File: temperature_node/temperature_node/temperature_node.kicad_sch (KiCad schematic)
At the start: 36 parts, among them J1 USB_C_Receptacle_USB2.0_16P, J2 S2B-PH-K-S, U1 ESP32-C3-WROOM-02, U2 SHT40-AD1B-R3, U3 MCP73831-2-OT, U4 USBLC6-2P6, U5 MIC5504-3.3YM5

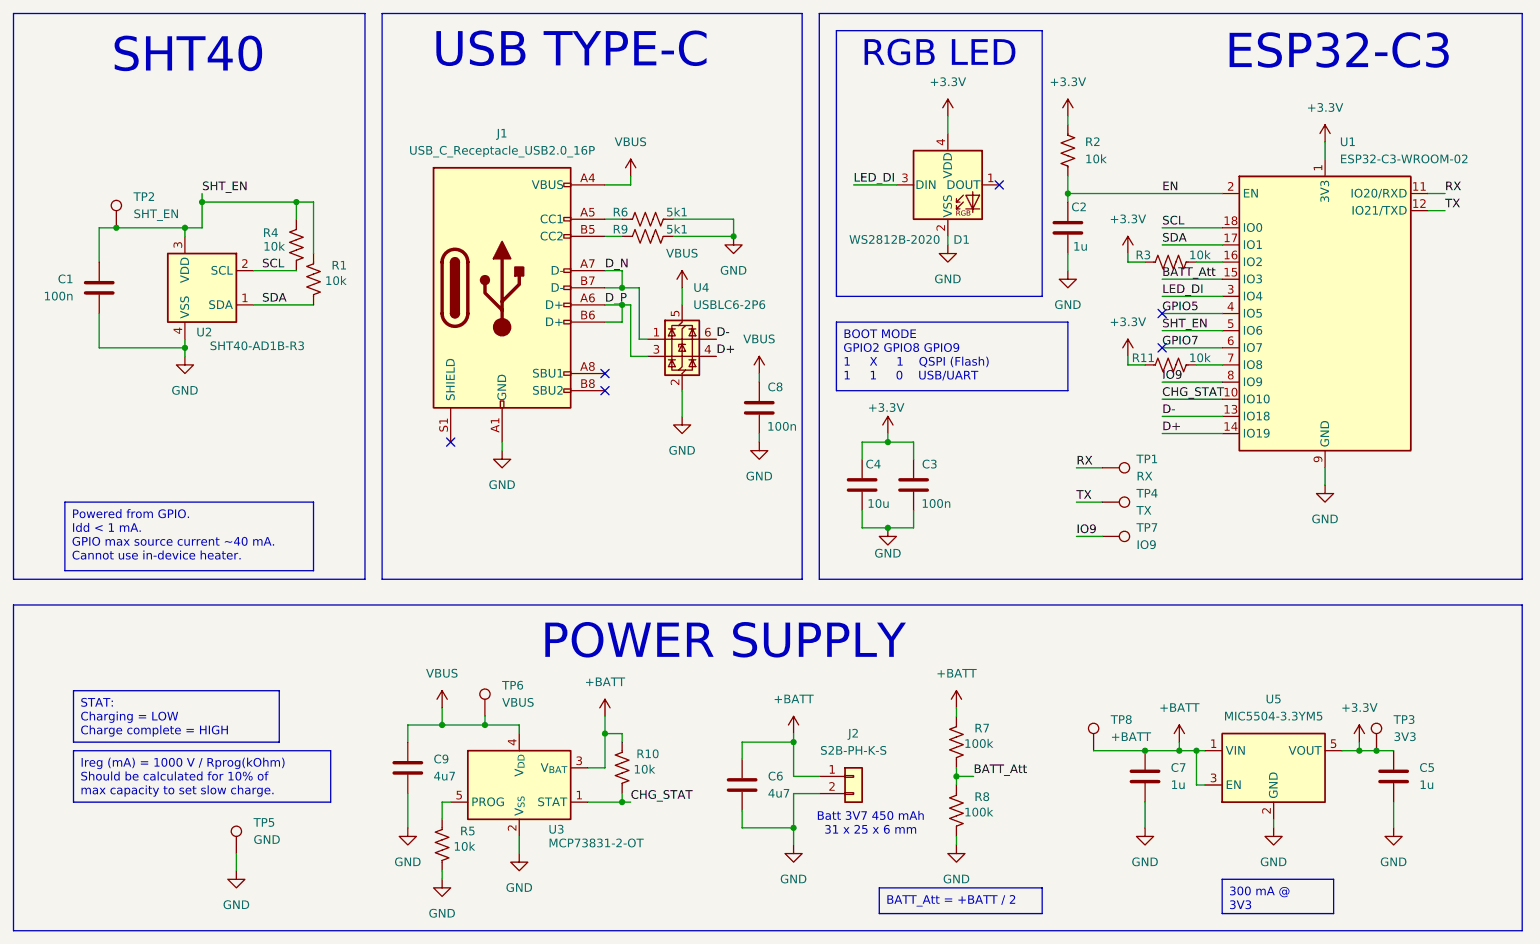
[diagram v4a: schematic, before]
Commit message: Add parameter for BOM and change some cap sizes for better availability
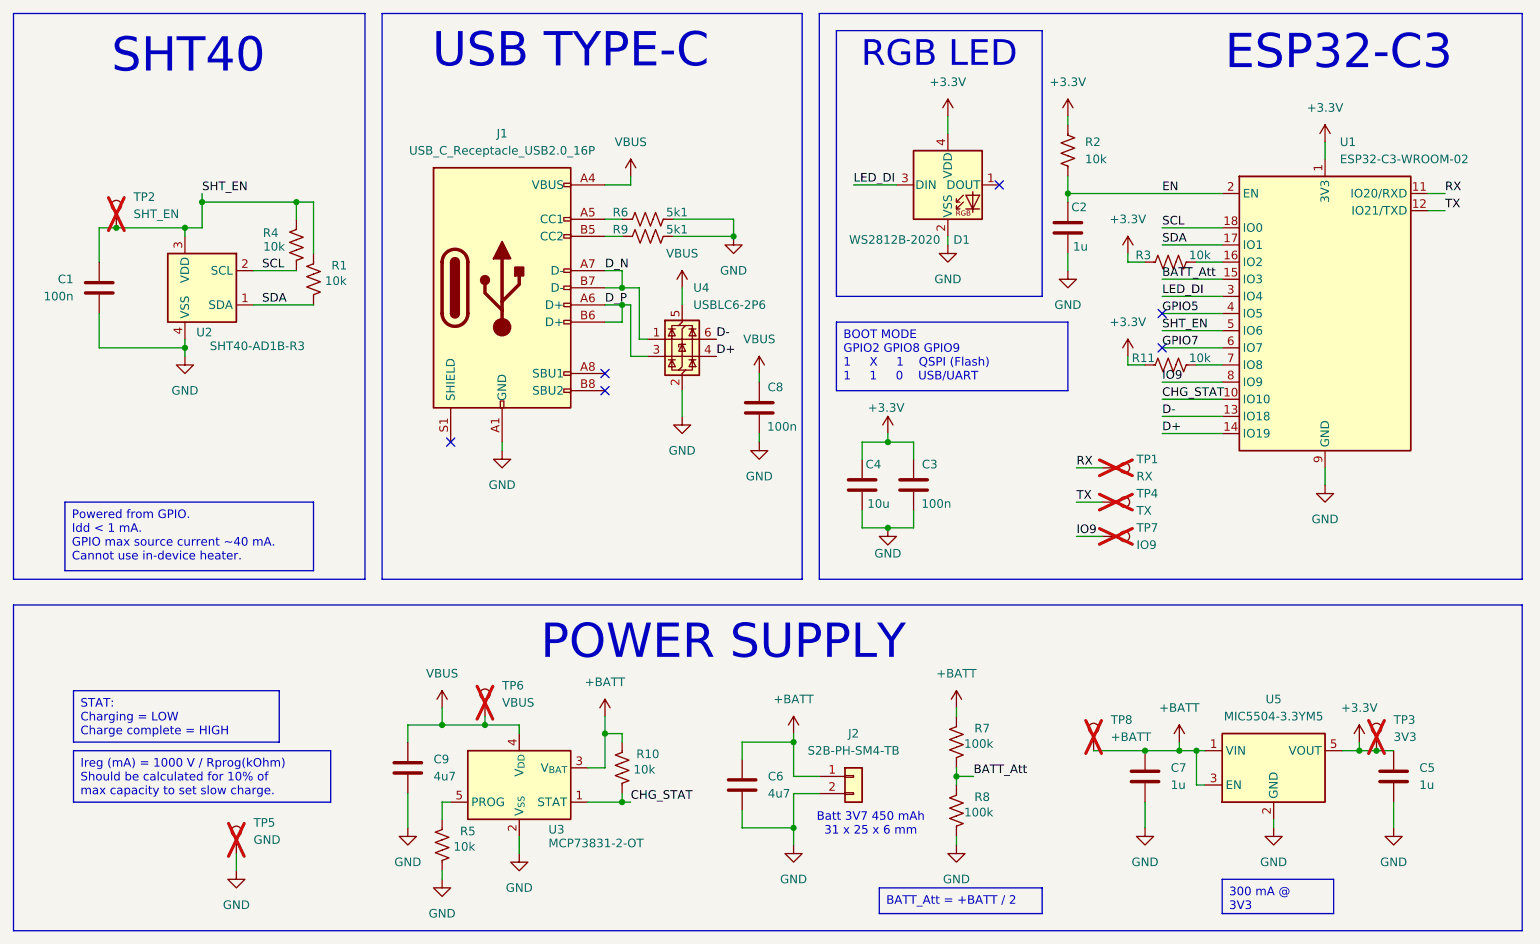
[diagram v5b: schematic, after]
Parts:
- C1, C2, C3, C5, C7, C8: LCSC PN (none) -> C60474
- C4: footprint Capacitor_SMD:C_0402_1005Metric -> Capacitor_SMD:C_0805_2012Metric; LCSC PN (none) -> C17024
- C6, C9: footprint Capacitor_SMD:C_0402_1005Metric -> Capacitor_SMD:C_0603_1608Metric; LCSC PN (none) -> C913474
- D1: LCSC PN (none) -> C965555
- J1: LCSC PN (none) -> C5143397
- J2: value S2B-PH-K-S -> S2B-PH-SM4-TB; LCSC PN (none) -> C295747
- R1, R10, R11, R2, R3, R4, R5: LCSC PN (none) -> C723366
- R6, R9: LCSC PN (none) -> C25905
- R7, R8: LCSC PN (none) -> C102760
- TP1, TP2, TP3, TP4, TP5, TP6, TP7, TP8: now not fitted
- U1: LCSC PN (none) -> C2934560
- U3: LCSC PN (none) -> C150772
- U4: LCSC PN (none) -> C2827693
- U5: LCSC PN (none) -> C3021093
